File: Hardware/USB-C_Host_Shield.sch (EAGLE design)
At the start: 39 parts, among them J1 USB-C, J2 GPIN, J3 GPOUT, J4 Power Select, U1 ARDUINO_UNO_R3_SHIELDBASIC, U2 LM1117, U3 74HC4050, U5 MAX3421, U6 3.3V/150mA, Y1 12.0mhZ

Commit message: Completed action items
Finished routing after adjusting design to comply with ERC and DRC.
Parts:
- added D2: 1A/15V/220mV, SparkFun-DiscreteSemi:DIODE-SCHOTTKY-LSM115JE3
- S1: value (none) -> Main Power
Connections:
- removed net N$2: S1.S
- new net N$5: D2.C, F1.2
- new net VDD: D2.A, J4.2, R10.2, R9.2, S1.P
- net GND: now also S1.S
- net POWER_IN: no longer F1.2, J4.2, R10.2, R9.2, S1.P
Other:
- moved on the sheet: S1
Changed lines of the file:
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@@
 <part name="JP1" library="SparkFun-Jumpers" deviceset="JUMPER-SMT_2_NC_TRACE" device="_SILK" package3d_urn="urn:adsk.eagle:package:39281/1"/>
 <part name="J4" library="SparkFun-Connectors" deviceset="CONN_03" device="" value="Power Select"/>
-<part name="S1" library="SparkFun-Switches" deviceset="SWITCH-SPDT" device="-SMD-AYZ0202"/>
+<part name="S1" library="SparkFun-Switches" deviceset="SWITCH-SPDT" device="-SMD-AYZ0202" value="Main Power"/>
 <part name="R9" library="SparkFun-Resistors" deviceset="56KOHM" device="" value="56k"/>
 <part name="R10" library="SparkFun-Resistors" deviceset="56KOHM" device="" value="56k"/>
+<part name="SUPPLY10" library="SparkFun-PowerSymbols" deviceset="VDD" device=""/>
+<part name="SUPPLY11" library="SparkFun-PowerSymbols" deviceset="VDD" device=""/>
+<part name="SUPPLY3" library="SparkFun-PowerSymbols" deviceset="VDD" device=""/>
+<part name="SUPPLY12" library="SparkFun-PowerSymbols" deviceset="VDD" device=""/>
+<part name="SUPPLY13" library="SparkFun-PowerSymbols" deviceset="VDD" device=""/>
+<part name="GND11" library="SparkFun-PowerSymbols" deviceset="GND" device=""/>
+<part name="D2" library="SparkFun-DiscreteSemi" deviceset="DIODE-SCHOTTKY" device="-LSM115JE3" value="1A/15V/220mV"/>
 </parts>
 <sheets>
@@
 <attribute name="NAME" x="88.9" y="154.432" size="1.778" layer="95" font="vector" rot="R180"/>
 </instance>
-<instance part="S1" gate="1" x="116.84" y="157.48" smashed="yes">
-<attribute name="NAME" x="118.11" y="160.528" size="1.778" layer="95" font="vector" align="bottom-center"/>
-<attribute name="VALUE" x="117.856" y="154.178" size="1.778" layer="96" font="vector" align="top-center"/>
+<instance part="S1" gate="1" x="114.3" y="157.48" smashed="yes">
+<attribute name="NAME" x="115.57" y="163.576" size="1.778" layer="95" font="vector" align="bottom-center"/>
+<attribute name="VALUE" x="116.84" y="162.814" size="1.778" layer="96" font="vector" align="top-center"/>
 </instance>
 <instance part="R9" gate="G$1" x="33.02" y="78.74" smashed="yes" rot="R90">
@@
 <attribute name="NAME" x="36.576" y="76.2" size="1.778" layer="95" font="vector" rot="R90" align="bottom-center"/>
 <attribute name="VALUE" x="34.544" y="83.82" size="1.778" layer="96" font="vector" rot="R90" align="top-center"/>
+</instance>
+<instance part="SUPPLY10" gate="VDD" x="63.5" y="165.1" smashed="yes">
+<attribute name="VALUE" x="63.5" y="167.894" size="1.778" layer="96" font="vector" align="bottom-center"/>
+</instance>
+<instance part="SUPPLY11" gate="VDD" x="106.68" y="162.56" smashed="yes">
+<attribute name="VALUE" x="106.68" y="165.354" size="1.778" layer="96" font="vector" align="bottom-center"/>
+</instance>
+<instance part="SUPPLY3" gate="VDD" x="20.32" y="91.44" smashed="yes">
+<attribute name="VALUE" x="20.32" y="94.234" size="1.778" layer="96" font="vector" align="bottom-center"/>
+</instance>
+<instance part="SUPPLY12" gate="VDD" x="33.02" y="88.9" smashed="yes">
+<attribute name="VALUE" x="33.02" y="91.694" size="1.778" layer="96" font="vector" align="bottom-center"/>
+</instance>
+<instance part="SUPPLY13" gate="VDD" x="38.1" y="88.9" smashed="yes">
+<attribute name="VALUE" x="38.1" y="91.694" size="1.778" layer="96" font="vector" align="bottom-center"/>
+</instance>
+<instance part="GND11" gate="1" x="121.92" y="149.86" smashed="yes">
+<attribute name="VALUE" x="121.92" y="149.606" size="1.778" layer="96" font="vector" align="top-center"/>
+</instance>
+<instance part="D2" gate="G$1" x="20.32" y="86.36" smashed="yes" rot="R270">
+<attribute name="NAME" x="17.272" y="88.9" size="1.778" layer="95" font="vector" rot="R270"/>
+<attribute name="VALUE" x="18.288" y="88.9" size="1.778" layer="96" font="vector" rot="R270" align="top-left" display="off"/>
 </instance>
 </instances>
@@
 <pinref part="JP1" gate="G$1" pin="1"/>
 </segment>
+<segment>
+<pinref part="S1" gate="1" pin="S"/>
+<wire x1="121.92" y1="154.94" x2="119.38" y2="154.94" width="0.1524" layer="91"/>
+<wire x1="121.92" y1="154.94" x2="121.92" y2="152.4" width="0.1524" layer="91"/>
+<pinref part="GND11" gate="1" pin="GND"/>
+</segment>
 </net>
 <net name="N$7" class="0">
@@
 <wire x1="129.54" y1="154.94" x2="127" y2="154.94" width="0.1524" layer="91"/>
 <wire x1="127" y1="154.94" x2="127" y2="160.02" width="0.1524" layer="91"/>
-<wire x1="127" y1="160.02" x2="121.92" y2="160.02" width="0.1524" layer="91"/>
+<wire x1="127" y1="160.02" x2="119.38" y2="160.02" width="0.1524" layer="91"/>
 <junction x="127" y="160.02"/>
 <pinref part="S1" gate="1" pin="O"/>
-</segment>
-<segment>
-<pinref part="J4" gate="J$1" pin="2"/>
-<wire x1="78.74" y1="160.02" x2="68.58" y2="160.02" width="0.1524" layer="91"/>
-<label x="68.58" y="160.02" size="1.27" layer="95" font="vector"/>
-</segment>
-<segment>
-<pinref part="S1" gate="1" pin="P"/>
-<wire x1="114.3" y1="157.48" x2="104.14" y2="157.48" width="0.1524" layer="91"/>
-<label x="104.14" y="157.48" size="1.27" layer="95" font="vector"/>
-</segment>
-<segment>
-<pinref part="F1" gate="F1" pin="2"/>
-<wire x1="20.32" y1="81.28" x2="20.32" y2="83.82" width="0.1524" layer="91"/>
-<label x="20.32" y="83.82" size="1.27" layer="95" rot="R90" xref="yes"/>
-</segment>
-<segment>
-<pinref part="R9" gate="G$1" pin="2"/>
-<wire x1="33.02" y1="83.82" x2="33.02" y2="88.9" width="0.1524" layer="91"/>
-<label x="33.02" y="88.9" size="1.27" layer="95" rot="R90" xref="yes"/>
-</segment>
-<segment>
-<pinref part="R10" gate="G$1" pin="2"/>
-<wire x1="38.1" y1="83.82" x2="38.1" y2="88.9" width="0.1524" layer="91"/>
-<label x="38.1" y="88.9" size="1.27" layer="95" rot="R90" xref="yes"/>
 </segment>
 </net>
@@
 </segment>
 </net>
-<net name="N$2" class="0">
-<segment>
-<pinref part="S1" gate="1" pin="S"/>
-<wire x1="124.46" y1="154.94" x2="121.92" y2="154.94" width="0.1524" layer="91"/>
-<wire x1="124.46" y1="154.94" x2="124.46" y2="152.4" width="0.1524" layer="91"/>
+<net name="VDD" class="0">
+<segment>
+<pinref part="J4" gate="J$1" pin="2"/>
+<wire x1="78.74" y1="160.02" x2="63.5" y2="160.02" width="0.1524" layer="91"/>
+<wire x1="63.5" y1="160.02" x2="63.5" y2="165.1" width="0.1524" layer="91"/>
+<pinref part="SUPPLY10" gate="VDD" pin="VDD"/>
+</segment>
+<segment>
+<pinref part="S1" gate="1" pin="P"/>
+<wire x1="111.76" y1="157.48" x2="106.68" y2="157.48" width="0.1524" layer="91"/>
+<wire x1="106.68" y1="157.48" x2="106.68" y2="162.56" width="0.1524" layer="91"/>
+<pinref part="SUPPLY11" gate="VDD" pin="VDD"/>
+</segment>
+<segment>
+<pinref part="R9" gate="G$1" pin="2"/>
+<wire x1="33.02" y1="83.82" x2="33.02" y2="88.9" width="0.1524" layer="91"/>
+<pinref part="SUPPLY12" gate="VDD" pin="VDD"/>
+</segment>
+<segment>
+<pinref part="R10" gate="G$1" pin="2"/>
+<wire x1="38.1" y1="83.82" x2="38.1" y2="88.9" width="0.1524" layer="91"/>
+<pinref part="SUPPLY13" gate="VDD" pin="VDD"/>
+</segment>
+<segment>
+<pinref part="SUPPLY3" gate="VDD" pin="VDD"/>
+<wire x1="20.32" y1="91.44" x2="20.32" y2="88.9" width="0.1524" layer="91"/>
+<pinref part="D2" gate="G$1" pin="A"/>
+</segment>
+</net>
+<net name="N$5" class="0">
+<segment>
+<pinref part="F1" gate="F1" pin="2"/>
+<wire x1="20.32" y1="81.28" x2="20.32" y2="83.82" width="0.1524" layer="91"/>
+<pinref part="D2" gate="G$1" pin="C"/>
 </segment>
 </net>
@@
 </sheet>
 </sheets>
+<errors>
+</errors>
 </schematic>
 </drawing>

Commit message: Updates for design review
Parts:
- added LOGO1: OSHW-LOGOM, SparkFun-Aesthetics:OSHW-LOGOM
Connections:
- net GND: no longer S1.S
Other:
- note added: "Cut JP1 for Shield to not be connected to GND"
- note added: "Vin = 6.5V-16V"
- note removed: "Vin = 5V-16V"
- moved on the sheet: C10, JP1, R2, R6, S2, U1

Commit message: Further changes for design review made
Working through SF Board Checklist now
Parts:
- added LOGO2: SFE_LOGO_NAME_FLAME.1_INCH, SparkFun-Aesthetics:SFE_LOGO_NAME_FLAME.1_INCH
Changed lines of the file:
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@@
 <part name="LOGO1" library="SparkFun-Aesthetics" deviceset="OSHW-LOGO" device="M"/>
 <part name="SUPPLY15" library="SparkFun-PowerSymbols" deviceset="3.3V" device=""/>
+<part name="LOGO2" library="SparkFun-Aesthetics" deviceset="SFE_LOGO_NAME_FLAME" device=".1_INCH"/>
 </parts>
 <sheets>
@@
 <plain>
 <text x="165.608" y="11.43" size="2.54" layer="94" font="vector">M. Chodikov</text>
-<text x="239.268" y="6.35" size="2.54" layer="94">v01</text>
+<text x="239.268" y="6.35" size="2.54" layer="94" font="vector">v01</text>
 <text x="78.74" y="177.8" size="2.54" layer="94" font="vector">Power Select &amp; Regulator</text>
 <text x="190.5" y="106.68" size="2.54" layer="94" font="vector">Arduino Shield</text>
@@
 <wire x1="177.8" y1="114.3" x2="248.92" y2="114.3" width="0.2032" layer="94" style="shortdash"/>
 <text x="198.12" y="177.8" size="2.54" layer="94" font="vector">Hex Inverter</text>
-<text x="187.96" y="175.26" size="1.27" layer="97">Translate 5V Arduino signals to 3.3V for the MAX3421</text>
-<text x="78.74" y="144.78" size="1.27" layer="97">Use jumper to connect
+<text x="187.96" y="175.26" size="1.27" layer="97" font="vector">Translate 5V Arduino signals to 3.3V for the MAX3421</text>
+<text x="78.74" y="144.78" size="1.27" layer="97" font="vector">Use jumper to connect
 between 5V and Vin
 for boards power supply</text>
-<text x="20.32" y="167.64" size="1.27" layer="97">Vin = 6.5V-16V</text>
-<text x="7.62" y="30.48" size="1.27" layer="97">Cut JP1 for Shield to
+<text x="20.32" y="167.64" size="1.27" layer="97" font="vector">Vin = 6.5V-16V</text>
+<text x="7.62" y="30.48" size="1.27" layer="97" font="vector">Cut JP1 for Shield to
 not be connected
 to GND</text>
@@
 <instance part="U1" gate="G$1" x="200.66" y="81.28" smashed="yes">
 <attribute name="NAME" x="191.008" y="101.854" size="1.778" layer="95" font="vector"/>
-<attribute name="VALUE" x="191.77" y="55.626" size="1.778" layer="96" font="vector" align="top-left"/>
+<attribute name="VALUE" x="181.61" y="55.626" size="1.778" layer="96" font="vector" align="top-left"/>
 </instance>
 <instance part="J1" gate="J1" x="5.08" y="58.42" smashed="yes">
@@
 <attribute name="VALUE" x="63.5" y="89.154" size="1.778" layer="96" font="vector" align="bottom-center"/>
 </instance>
+<instance part="LOGO2" gate="G$1" x="190.5" y="33.02" smashed="yes"/>
 </instances>
 <busses>

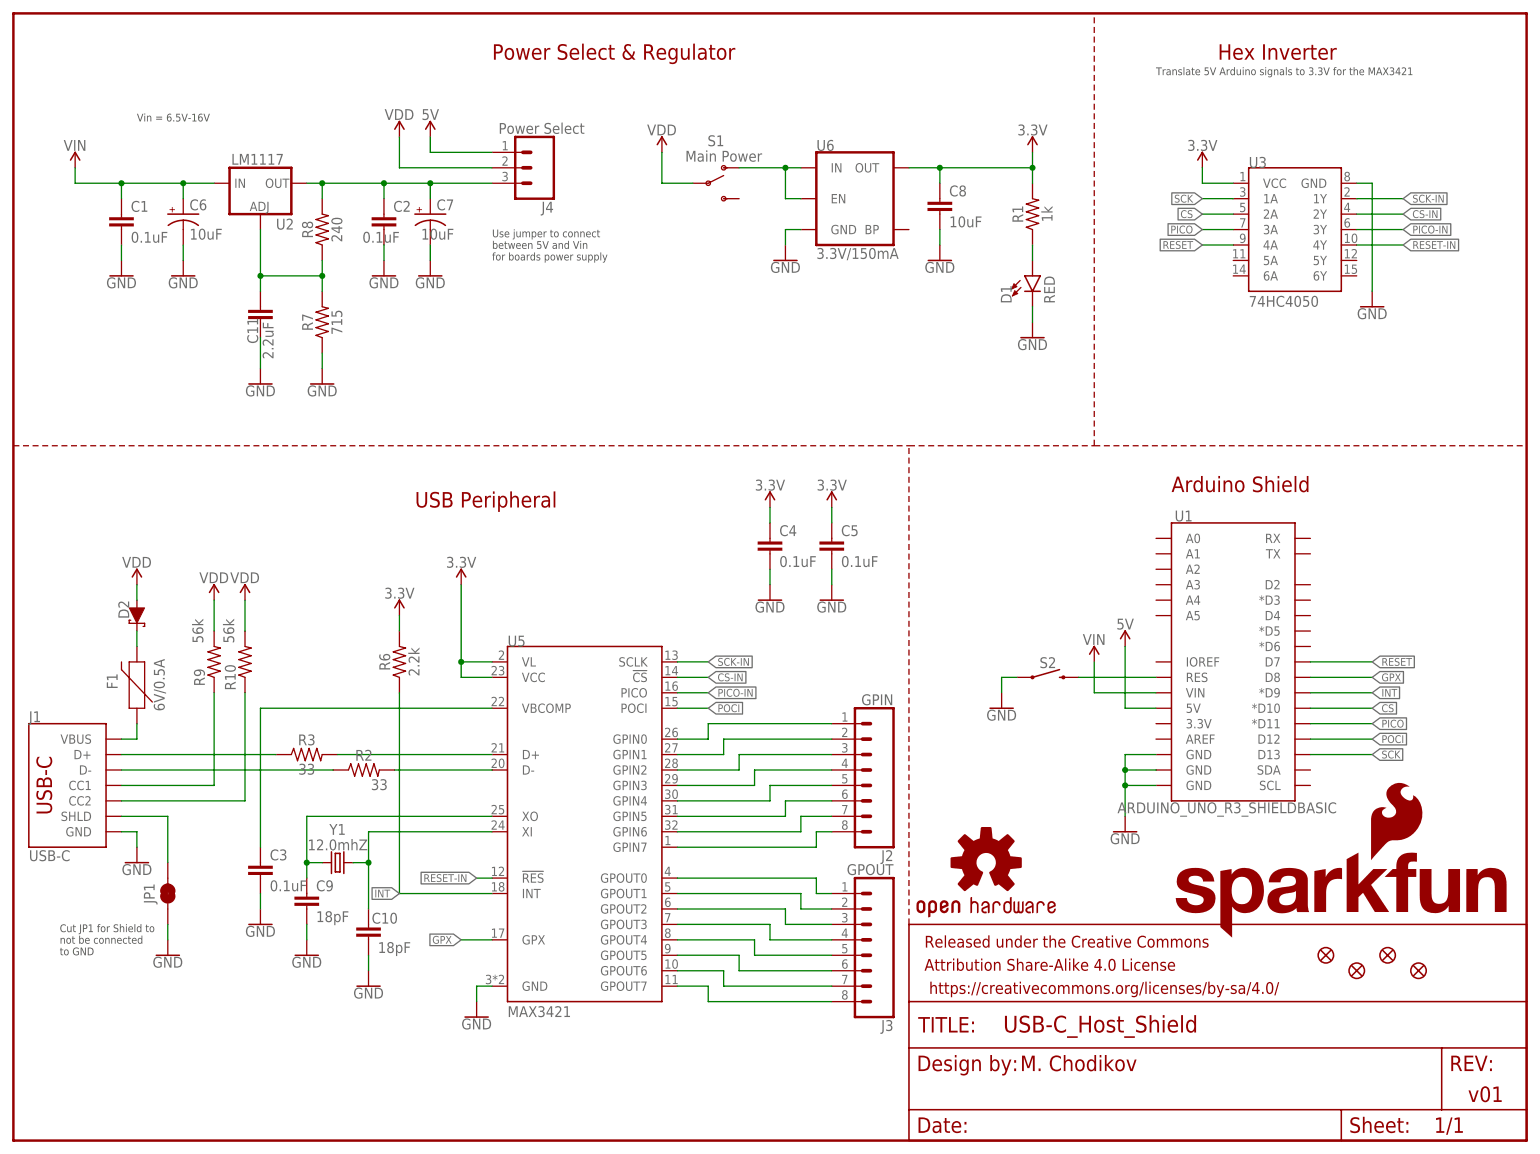
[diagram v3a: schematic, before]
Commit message: Updates for design review notes
Made more updates according to design review notes. Updated prod_id for the MAX3421
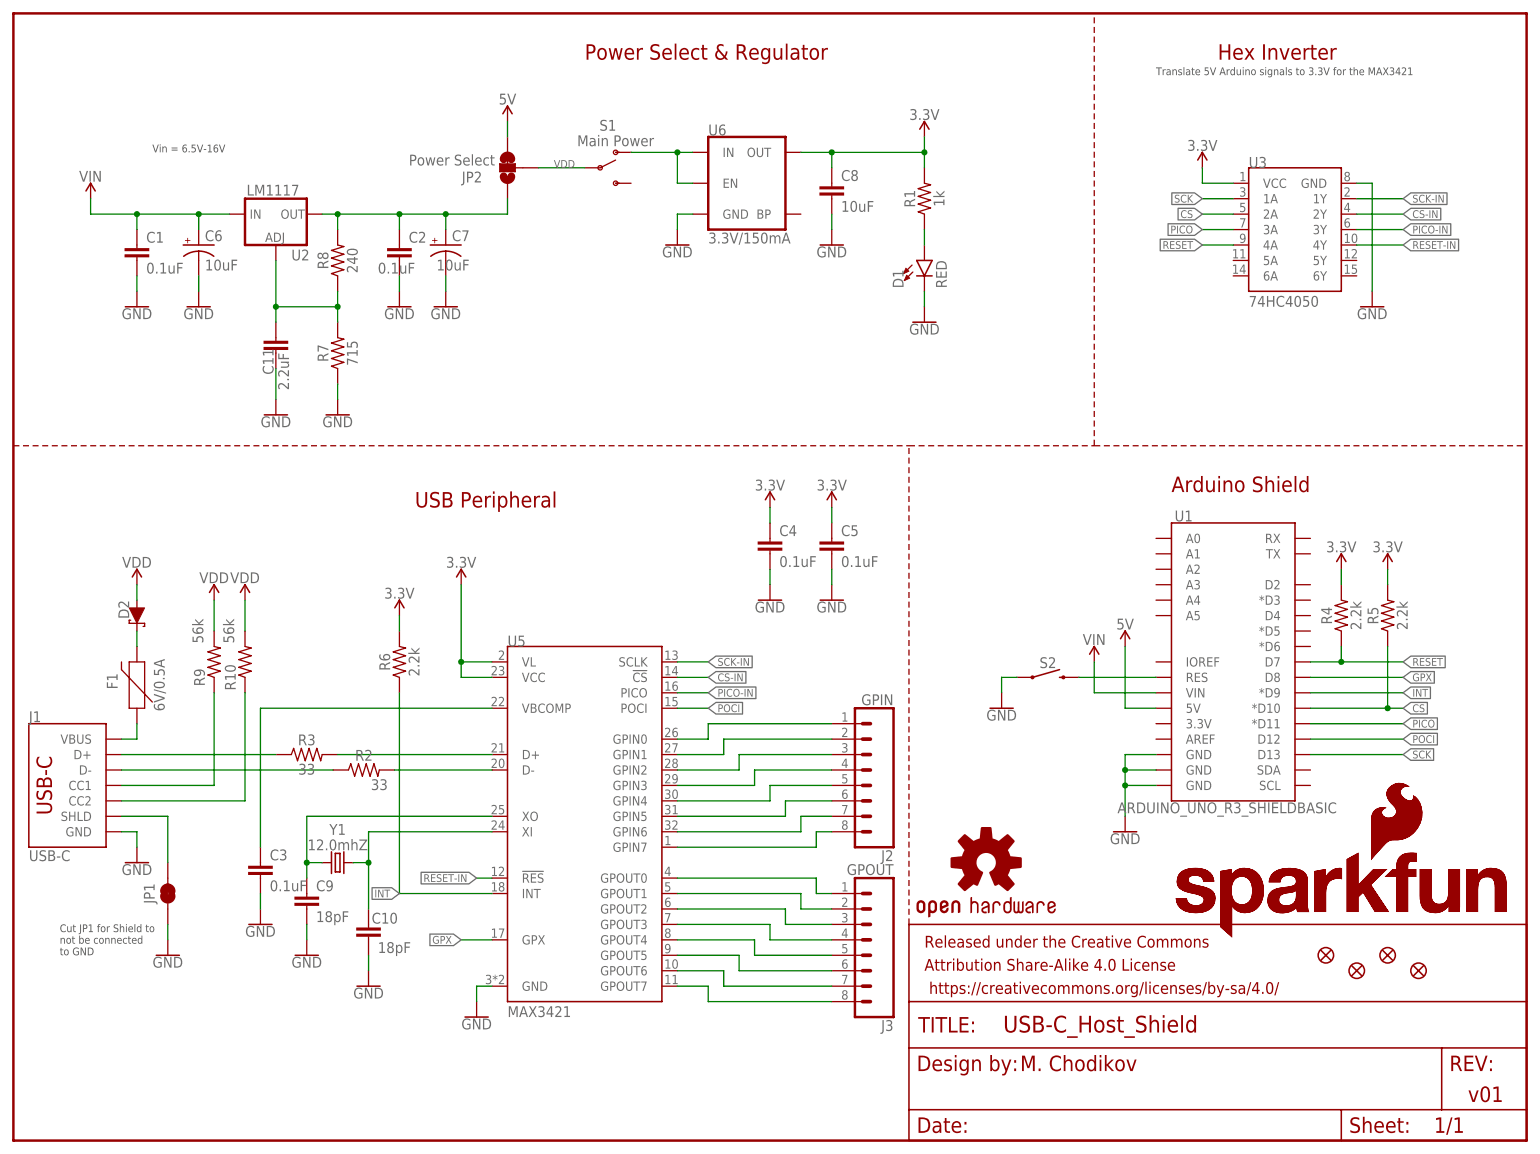
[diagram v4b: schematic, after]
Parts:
- removed J4: Power Select, SparkFun-Connectors:CONN_03
- added JP2: Power Select, SparkFun-Jumpers:JUMPER-SMT_3_1-NC_TRACE_SILK
- added LOGO3: SFE_LOGO_NAME_FLAME.2_INCH, SparkFun-Aesthetics:SFE_LOGO_NAME_FLAME.2_INCH
- added R4, R5: 2.2k, SparkFun-Resistors:2.2KOHM-0603-1/10W-1%
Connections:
- net 3.3V: now also R4.2, R5.2
- net 5V: now also JP2.3; no longer J4.1
- net CS: now also R5.1
- net N$6: now also JP2.1; no longer J4.3
- net RESET: now also R4.1
- net VDD: now also JP2.2; no longer J4.2
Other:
- note removed: "Use jumper to connect between 5V and Vin for boards power supply"
- moved on the sheet: C1, C11, C2, C6, C7, C8, D1, R1, R7, R8, S1, U2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

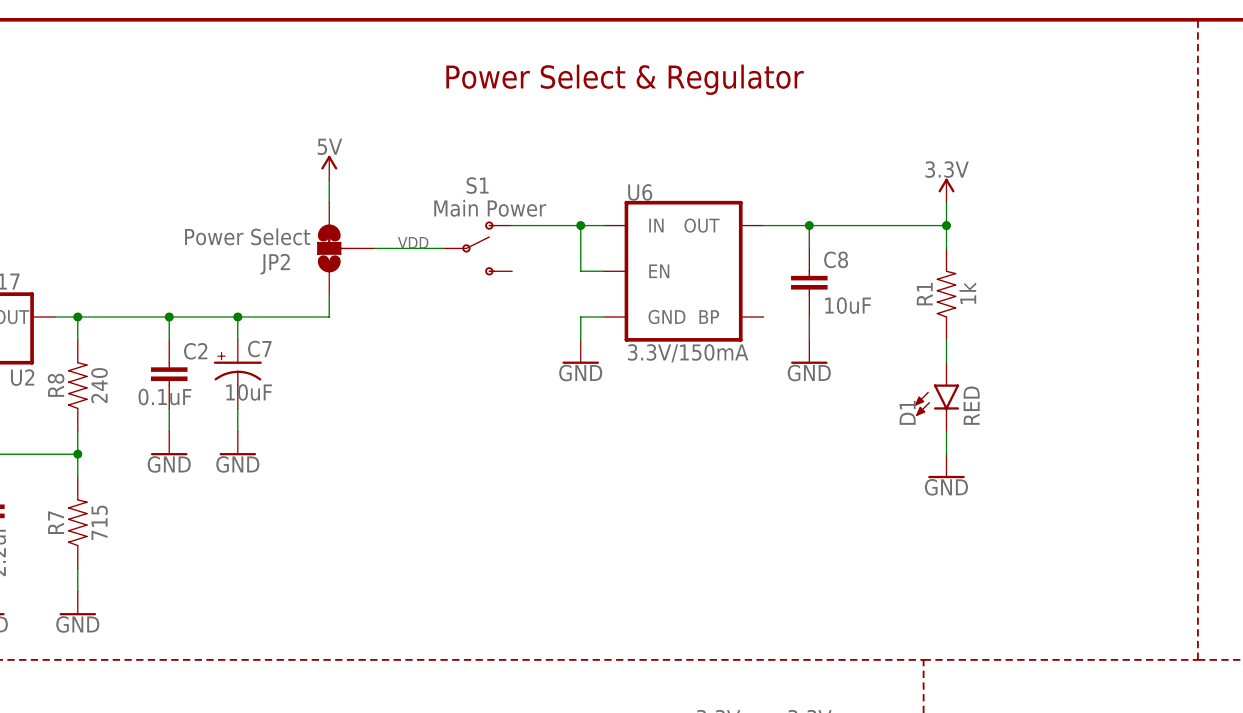
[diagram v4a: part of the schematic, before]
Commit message: Finalized schematic
Added new switch instead of trace jumper for power switch between VIN and 5V
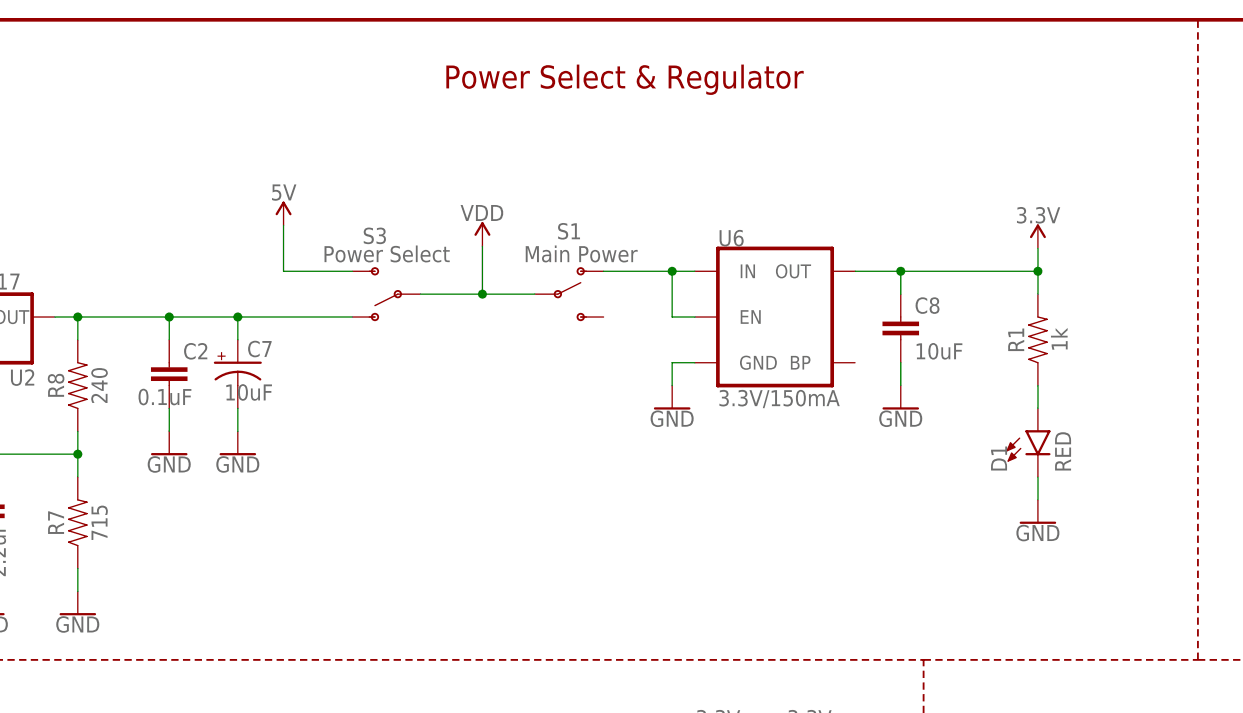
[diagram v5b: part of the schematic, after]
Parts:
- removed JP2: Power Select, SparkFun-Jumpers:JUMPER-SMT_3_1-NC_TRACE_SILK
- added S3: Power Select, SparkFun-Switches:SWITCH-SPDT-SMD-AYZ0202
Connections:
- net 5V: now also S3.S; no longer JP2.3
- net N$6: now also S3.O; no longer JP2.1
- net VDD: now also S3.P; no longer JP2.2
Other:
- moved on the sheet: C8, D1, R1, S1, U6
